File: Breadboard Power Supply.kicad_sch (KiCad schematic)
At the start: 34 parts, among them J1 USB-C Power Only, J10 Conn_01x02_Male, J11 Conn_01x02_Male, J2 Conn_01x02_Male, J3 Conn_01x02_Male, J4 Conn_01x02_Male, J5 Conn_01x02_Male, J6 Conn_01x02_Male, J7 Conn_01x02_Male, J8 Conn_01x02_Male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

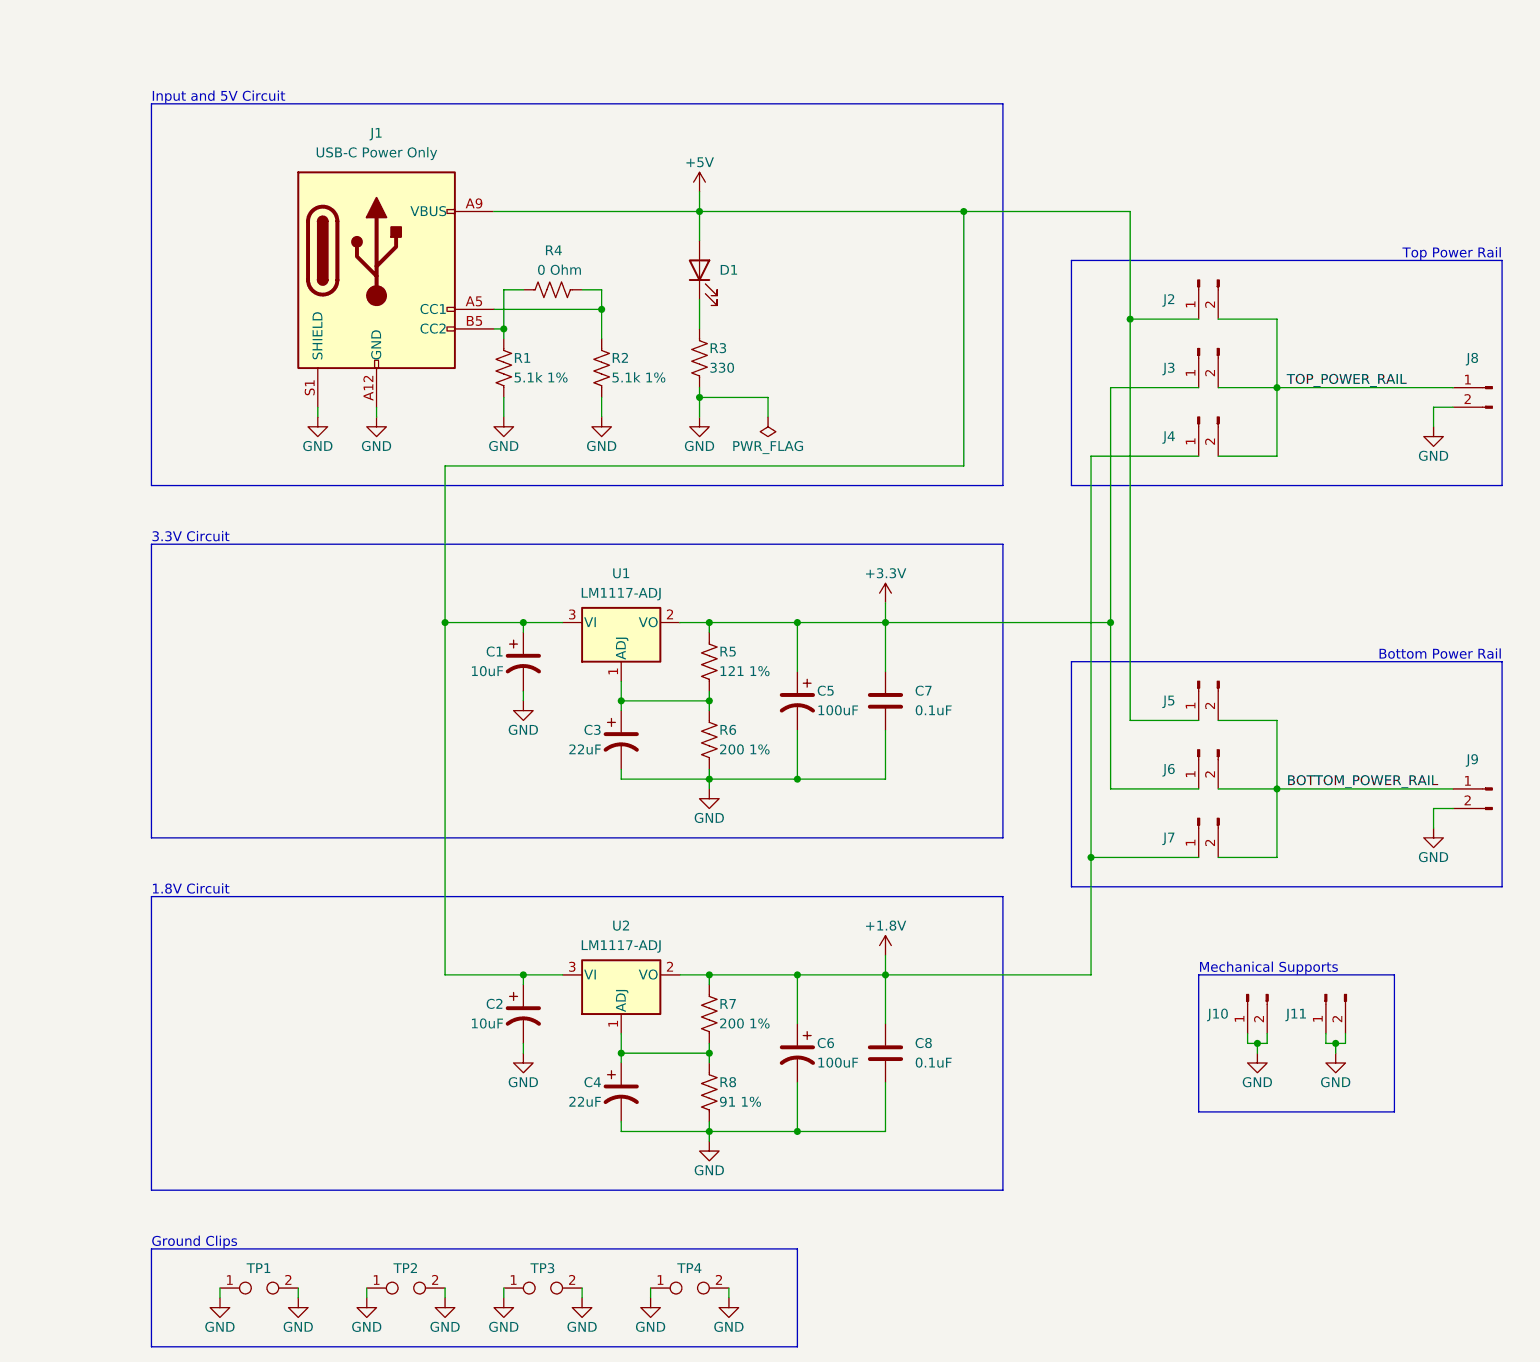
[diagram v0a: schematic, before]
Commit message: The power rails were mixed up.
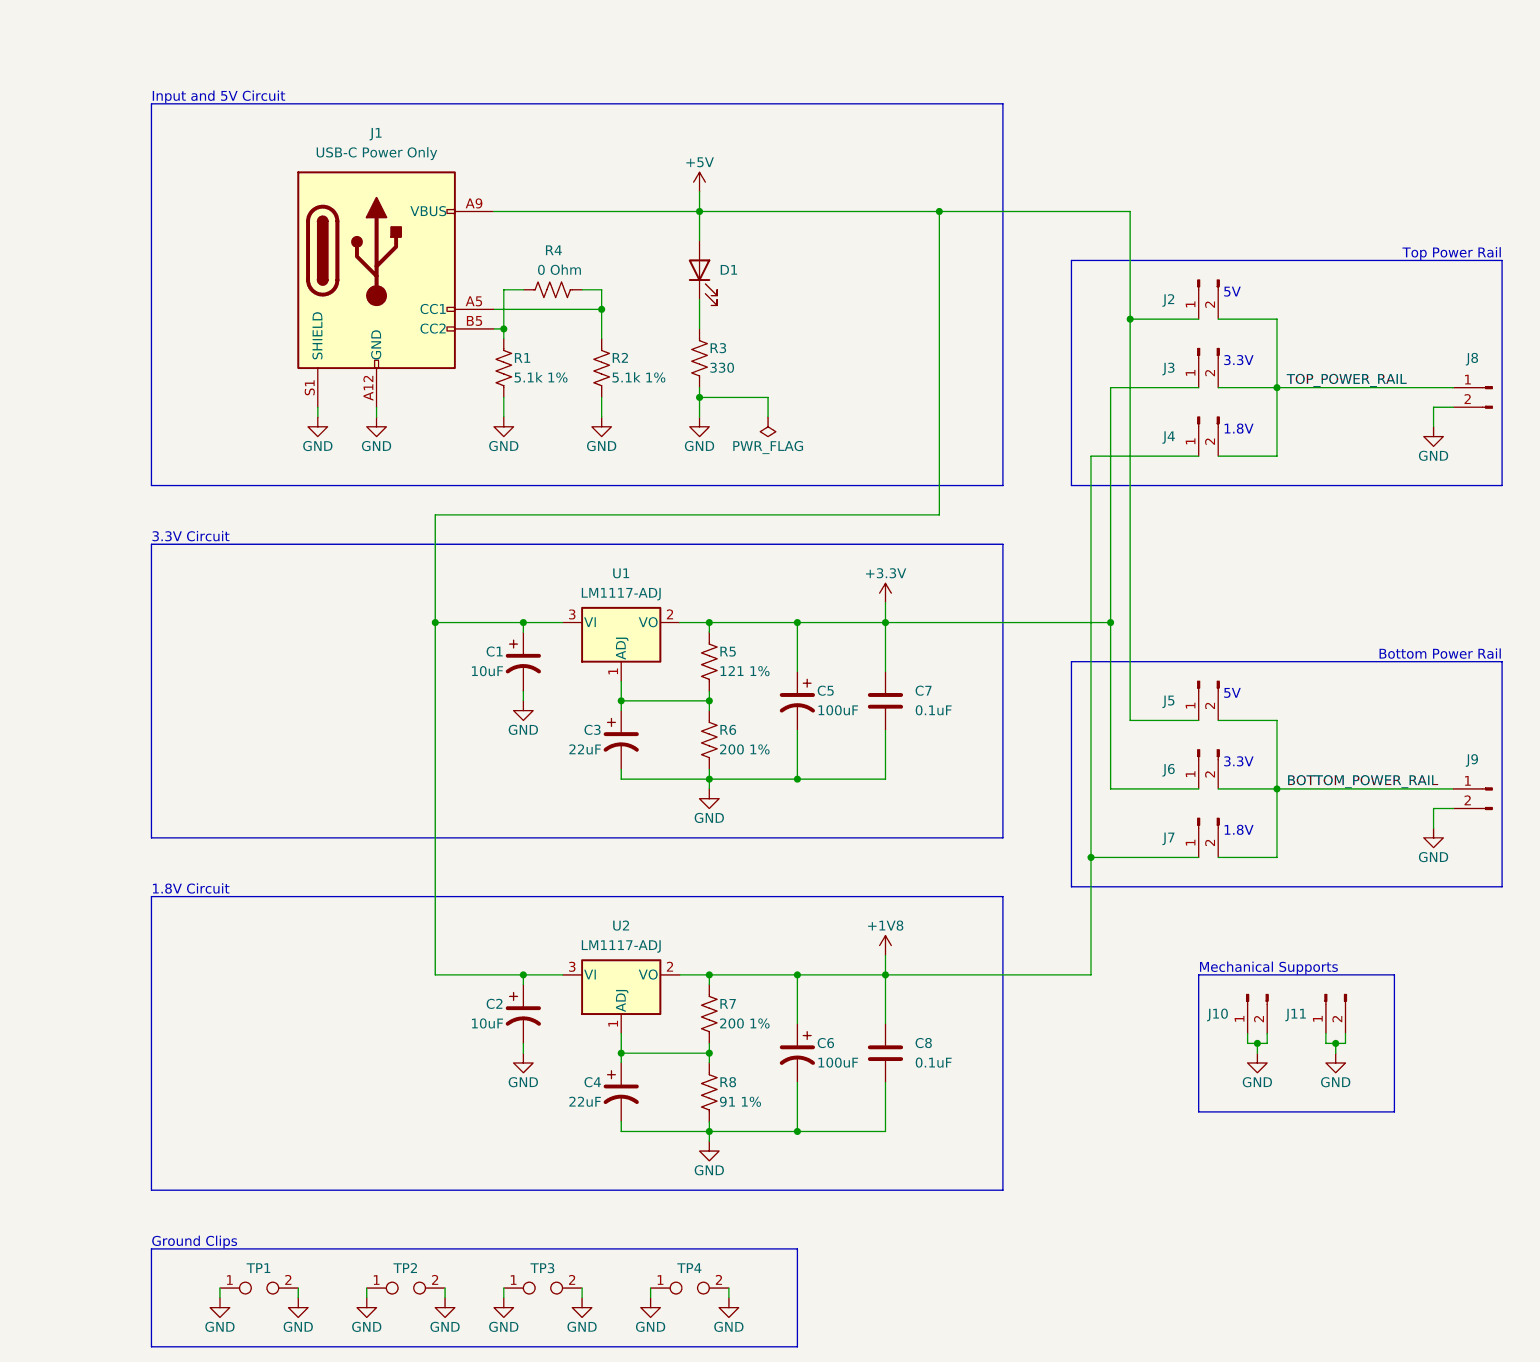
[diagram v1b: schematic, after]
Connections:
- net +3.3V: no longer C6.1, C8.1, J4.1 (Pin_1), J7.1 (Pin_1), R7.1, U2.2 (VO)
- new net +1V8: C6.1, C8.1, J4.1 (Pin_1), J7.1 (Pin_1), R7.1, U2.2 (VO)
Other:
- note added: "1.8V"
- note added: "3.3V"
- note added: "5V"

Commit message: Fixed an issue where the power rails were mixed up.
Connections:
- net +3.3V: no longer C1.1, C2.1, D1.2 (A), J1.A9 (VBUS), J1.B9 (VBUS), J2.1 (Pin_1), J5.1 (Pin_1), U1.3 (VI), U2.3 (VI)
- new net +5V: C1.1, C2.1, D1.2 (A), J1.A9 (VBUS), J1.B9 (VBUS), J2.1 (Pin_1), J5.1 (Pin_1), U1.3 (VI), U2.3 (VI)
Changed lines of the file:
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@@
-    )
-  )
-  (symbol (lib_id "power:+3.3V") (at 115.57 41.91 0) (mirror y) (unit 1)
-    (in_bom yes) (on_board yes) (dnp no)
-    (property "Reference" "#PWR03" (at 115.57 45.72 0)
-      (effects (font (size 1.27 1.27)) hide)
-    )
-    (property "Value" "+5V" (at 115.57 38.1 0)
-      (effects (font (size 1.27 1.27)))
-    )
-    (property "Footprint" "" (at 115.57 41.91 0)
-      (effects (font (size 1.27 1.27)) hide)
-    )
-    (property "Datasheet" "" (at 115.57 41.91 0)
-      (effects (font (size 1.27 1.27)) hide)
-    )
-    (pin "1")
-    (instances
-      (project "Breadboard Power Supply"
-        (path "/a474ae98-d5ea-4288-b242-cd0417157b2d"
-          (reference "#PWR03") (unit 1)
-        )
-      )
     )
   )
@@
         )
       )
+    )
+  )
+  (symbol (lib_id "power:+5V") (at 115.57 41.91 0) (unit 1)
+    (in_bom yes) (on_board yes) (dnp no) (fields_autoplaced)
+    (property "Reference" "#PWR03" (at 115.57 45.72 0)
+      (effects (font (size 1.27 1.27)) hide)
+    )
+    (property "Value" "+5V" (at 115.57 38.1 0)
+      (effects (font (size 1.27 1.27)))
+    )
+    (property "Footprint" "" (at 115.57 41.91 0)
+      (effects (font (size 1.27 1.27)) hide)
+    )
+    (property "Datasheet" "" (at 115.57 41.91 0)
+      (effects (font (size 1.27 1.27)) hide)
+    )
+    (pin "1")
+    (instances
+      (project "Breadboard Power Supply"
+        (path "/a474ae98-d5ea-4288-b242-cd0417157b2d"
+          (reference "#PWR03") (unit 1)
+        )
+      )

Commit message: Updates.
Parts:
- removed TP3, TP4: TestPoint_2Pole, Keystone 1287:1287, symbol Connector:TestPoint_2Pole
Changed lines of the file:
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@@
-    (stroke (width 0) (type default))
-  )
-  (wire (pts (xy 90.17 184.15) (xy 90.17 185.42))
     (stroke (width 0) (type default))
   )
@@
     (stroke (width 0) (type default))
   )
-  (wire (pts (xy 100.33 184.15) (xy 100.33 185.42))
-    (stroke (width 0) (type default))
-  )
   (wire (pts (xy 90.17 68.58) (xy 90.17 71.12))
     (stroke (width 0) (type default))
@@
     (stroke (width 0) (type default))
   )
-  (wire (pts (xy 109.22 184.15) (xy 109.22 185.42))
-    (stroke (width 0) (type default))
-  )
   (wire (pts (xy 115.57 44.45) (xy 115.57 41.91))
     (stroke (width 0) (type default))
@@
   )
   (wire (pts (xy 139.7 104.14) (xy 139.7 97.79))
-    (stroke (width 0) (type default))
-  )
-  (wire (pts (xy 119.38 184.15) (xy 119.38 185.42))
     (stroke (width 0) (type default))
   )
@@
     )
   )
-  (symbol (lib_id "power:GND") (at 100.33 185.42 0) (unit 1)
-    (in_bom yes) (on_board yes) (dnp no)
-    (property "Reference" "#PWR0123" (at 100.33 191.77 0)
-      (effects (font (size 1.27 1.27)) hide)
-    )
-    (property "Value" "GND" (at 100.33 189.23 0)
-      (effects (font (size 1.27 1.27)))
-    )
-    (property "Footprint" "" (at 100.33 185.42 0)
-      (effects (font (size 1.27 1.27)) hide)
-    )
-    (property "Datasheet" "" (at 100.33 185.42 0)
-      (effects (font (size 1.27 1.27)) hide)
-    )
-    (pin "1")
-    (instances
-      (project "Breadboard Power Supply"
-        (path "/a474ae98-d5ea-4288-b242-cd0417157b2d"
-          (reference "#PWR0123") (unit 1)
-        )
-      )
-    )
-  )
   (symbol (lib_id "Device:C_Polarized_US") (at 128.27 107.95 0) (mirror y) (unit 1)
     (in_bom yes) (on_board yes) (dnp no)
@@
     )
   )
-  (symbol (lib_id "power:GND") (at 109.22 185.42 0) (unit 1)
-    (in_bom yes) (on_board yes) (dnp no)
-    (property "Reference" "#PWR0120" (at 109.22 191.77 0)
-      (effects (font (size 1.27 1.27)) hide)
-    )
-    (property "Value" "GND" (at 109.22 189.23 0)
-      (effects (font (size 1.27 1.27)))
-    )
-    (property "Footprint" "" (at 109.22 185.42 0)
-      (effects (font (size 1.27 1.27)) hide)
-    )
-    (property "Datasheet" "" (at 109.22 185.42 0)
-      (effects (font (size 1.27 1.27)) hide)
-    )
-    (pin "1")
-    (instances
-      (project "Breadboard Power Supply"
-        (path "/a474ae98-d5ea-4288-b242-cd0417157b2d"
-          (reference "#PWR0120") (unit 1)
-        )
-      )
-    )
-  )
   (symbol (lib_id "power:GND") (at 63.5 185.42 0) (unit 1)
     (in_bom yes) (on_board yes) (dnp no)
@@
     )
   )
-  (symbol (lib_id "power:GND") (at 119.38 185.42 0) (unit 1)
-    (in_bom yes) (on_board yes) (dnp no)
-    (property "Reference" "#PWR0121" (at 119.38 191.77 0)
-      (effects (font (size 1.27 1.27)) hide)
-    )
-    (property "Value" "GND" (at 119.38 189.23 0)
-      (effects (font (size 1.27 1.27)))
-    )
-    (property "Footprint" "" (at 119.38 185.42 0)
-      (effects (font (size 1.27 1.27)) hide)
-    )
-    (property "Datasheet" "" (at 119.38 185.42 0)
-      (effects (font (size 1.27 1.27)) hide)
-    )
-    (pin "1")
-    (instances
-      (project "Breadboard Power Supply"
-        (path "/a474ae98-d5ea-4288-b242-cd0417157b2d"
-          (reference "#PWR0121") (unit 1)
-        )
-      )
-    )
-  )
   (symbol (lib_id "Connector:Conn_01x02_Male") (at 218.44 119.38 0) (mirror y) (unit 1)
     (in_bom yes) (on_board yes) (dnp no)
@@
         (path "/a474ae98-d5ea-4288-b242-cd0417157b2d"
           (reference "J9") (unit 1)
-        )
-      )
-    )
-  )
-  (symbol (lib_id "Connector:TestPoint_2Pole") (at 95.25 184.15 0) (unit 1)
-    (in_bom yes) (on_board yes) (dnp no)
-    (property "Reference" "TP3" (at 95.25 181.61 0)
-      (effects (font (size 1.27 1.27)))
-    )
-    (property "Value" "TestPoint_2Pole" (at 95.25 181.61 0)
-      (effects (font (size 1.27 1.27)) hide)
-    )
-    (property "Footprint" "Keystone 1287:1287" (at 95.25 184.15 0)
-      (effects (font (size 1.27 1.27)) hide)
-    )
-    (property "Datasheet" "https://www.keyelco.com/product.cfm/Vertical-Mount/1287/product_id/610" (at 95.25 184.15 0)
-      (effects (font (size 1.27 1.27)) hide)
-    )
-    (property "Silkscreen" "Ground" (at 95.25 184.15 0)
-      (effects (font (size 1.27 1.27)) hide)
-    )
-    (property "Digi-Key Part Num" "36-1287-ND" (at 95.25 184.15 0)
-      (effects (font (size 1.27 1.27)) hide)
-    )
-    (pin "1")
-    (pin "2")
-    (instances
-      (project "Breadboard Power Supply"
-        (path "/a474ae98-d5ea-4288-b242-cd0417157b2d"
-          (reference "TP3") (unit 1)
         )
       )
@@
     )
   )
-  (symbol (lib_id "power:GND") (at 90.17 185.42 0) (unit 1)
-    (in_bom yes) (on_board yes) (dnp no)
-    (property "Reference" "#PWR0119" (at 90.17 191.77 0)
-      (effects (font (size 1.27 1.27)) hide)
-    )
-    (property "Value" "GND" (at 90.17 189.23 0)
-      (effects (font (size 1.27 1.27)))
-    )
-    (property "Footprint" "" (at 90.17 185.42 0)
-      (effects (font (size 1.27 1.27)) hide)
-    )
-    (property "Datasheet" "" (at 90.17 185.42 0)
-      (effects (font (size 1.27 1.27)) hide)
-    )
-    (pin "1")
-    (instances
-      (project "Breadboard Power Supply"
-        (path "/a474ae98-d5ea-4288-b242-cd0417157b2d"
-          (reference "#PWR0119") (unit 1)
-        )
-      )
-    )
-  )
   (symbol (lib_id "Connector:Conn_01x02_Male") (at 218.44 67.31 0) (mirror y) (unit 1)
     (in_bom yes) (on_board yes) (dnp no)
@@
         )
       )
-    )
-  )
-  (symbol (lib_id "Connector:TestPoint_2Pole") (at 114.3 184.15 0) (unit 1)
-    (in_bom yes) (on_board yes) (dnp no)
-    (property "Reference" "TP4" (at 114.3 181.61 0)
-      (effects (font (size 1.27 1.27)))
-    )
-    (property "Value" "TestPoint_2Pole" (at 114.3 181.61 0)
-      (effects (font (size 1.27 1.27)) hide)
-    )
-    (property "Footprint" "Keystone 1287:1287" (at 114.3 184.15 0)
-      (effects (font (size 1.27 1.27)) hide)
-    )
-    (property "Datasheet" "https://www.keyelco.com/product.cfm/Vertical-Mount/1287/product_id/610" (at 114.3 184.15 0)
-      (effects (font (size 1.27 1.27)) hide)
-    )
-    (property "Silkscreen" "Ground" (at 114.3 184.15 0)
-      (effects (font (size 1.27 1.27)) hide)
-    )
-    (property "Digi-Key Part Num" "36-1287-ND" (at 114.3 184.15 0)
-      (effects (font (size 1.27 1.27)) hide)
-    )
-    (pin "1")
-    (pin "2")
-    (instances
-      (project "Breadboard Power Supply"
-        (path "/a474ae98-d5ea-4288-b242-cd0417157b2d"
-          (reference "TP4") (unit 1)
-        )
-      )

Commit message: Updates.
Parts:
- added VR1: LM1117MPX-3.3/NOPB, VREG_LM1117MPX-3.3/NOPB, symbol LM1117MPX-3.3_NOPB:LM1117MPX-3.3/NOPB
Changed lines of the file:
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@@
+    )
+  )
+  (symbol (lib_id "LM1117MPX-3.3_NOPB:LM1117MPX-3.3{slash}NOPB") (at 204.851 29.591 0) (unit 1)
+    (in_bom yes) (on_board yes) (dnp no) (fields_autoplaced)
+    (property "Reference" "VR1" (at 204.851 20.32 0)
+      (effects (font (size 1.27 1.27)))
+    )
+    (property "Value" "LM1117MPX-3.3/NOPB" (at 204.851 22.86 0)
+      (effects (font (size 1.27 1.27)))
+    )
+    (property "Footprint" "VREG_LM1117MPX-3.3/NOPB" (at 204.851 29.591 0)
+      (effects (font (size 1.27 1.27)) (justify bottom) hide)
+    )
+    (property "Datasheet" "" (at 204.851 29.591 0)
+      (effects (font (size 1.27 1.27)) hide)
+    )
+    (property "MAXIMUM_PACKAGE_HEIGHT" "1.80 mm" (at 204.851 29.591 0)
+      (effects (font (size 1.27 1.27)) (justify bottom) hide)
+    )
+    (property "STANDARD" "Manufacturer Recommendation" (at 204.851 29.591 0)
+      (effects (font (size 1.27 1.27)) (justify bottom) hide)
+    )
+    (property "PARTREV" "O" (at 204.851 29.591 0)
+      (effects (font (size 1.27 1.27)) (justify bottom) hide)
+    )
+    (property "MANUFACTURER" "Texas Instruments" (at 204.851 29.591 0)
+      (effects (font (size 1.27 1.27)) (justify bottom) hide)
+    )
+    (pin "1")
+    (pin "2")
+    (pin "3")
+    (pin "4")
+    (instances
+      (project "Breadboard Power Supply"
+        (path "/a474ae98-d5ea-4288-b242-cd0417157b2d"
+          (reference "VR1") (unit 1)
+        )
+      )
     )
   )
